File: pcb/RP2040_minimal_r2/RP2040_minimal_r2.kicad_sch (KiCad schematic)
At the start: 34 parts, among them J1 USB_B_Micro, J2 Conn_01x02, J3 Conn_02x18_Odd_Even, J4 Conn_02x18_Odd_Even, U1 NCP1117-3.3_SOT223, U2 W25Q128JVS, U3 RP2040, Y1 ABM8-272-T3

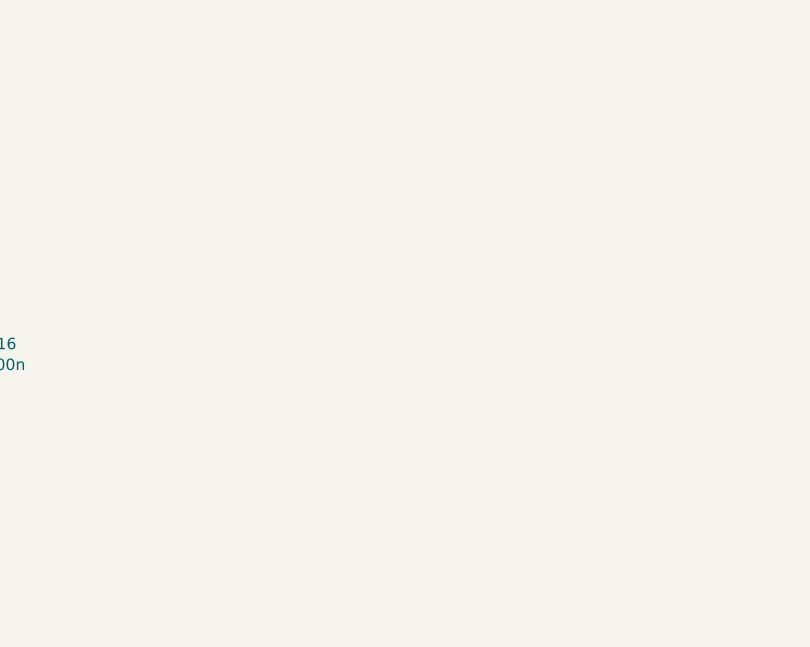
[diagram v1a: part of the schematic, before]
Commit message: add ddr contacts to pcb
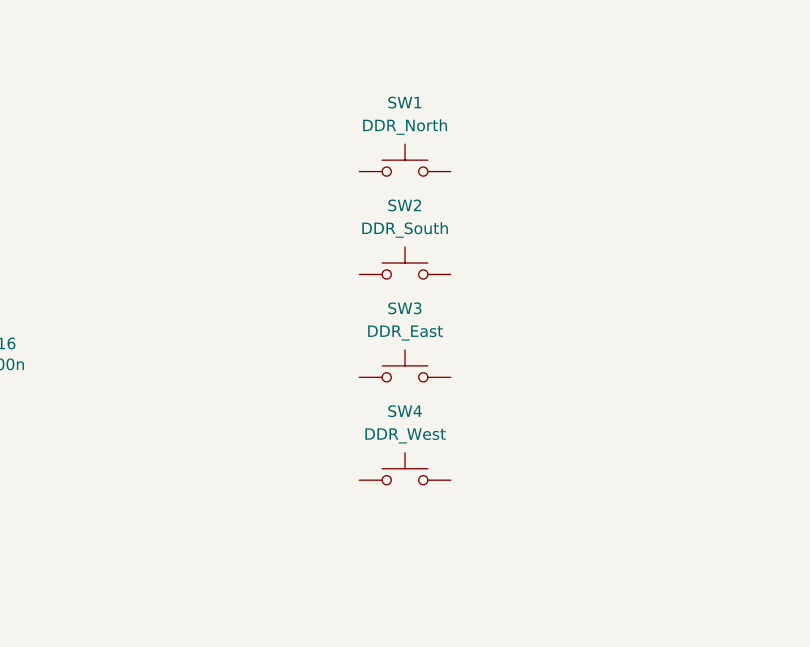
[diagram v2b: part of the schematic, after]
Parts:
- added SW1: DDR_North, Andrews_Library:DDR_CONTACT, symbol Switch:SW_Push
- added SW2: DDR_South, Andrews_Library:DDR_CONTACT, symbol Switch:SW_Push
- added SW3: DDR_East, Andrews_Library:DDR_CONTACT, symbol Switch:SW_Push
- added SW4: DDR_West, Andrews_Library:DDR_CONTACT, symbol Switch:SW_Push

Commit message: clean up pcb
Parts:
- removed H1, H2, H3, H4: MountingHole, MountingHole:MountingHole_2.7mm_M2.5, symbol Mechanical:MountingHole
- removed J3, J4: Conn_02x18_Odd_Even, Connector_PinHeader_2.54mm:PinHeader_2x18_P2.54mm_Vertical, symbol Connector_Generic:Conn_02x18_Odd_Even
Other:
- note removed: "IOs"

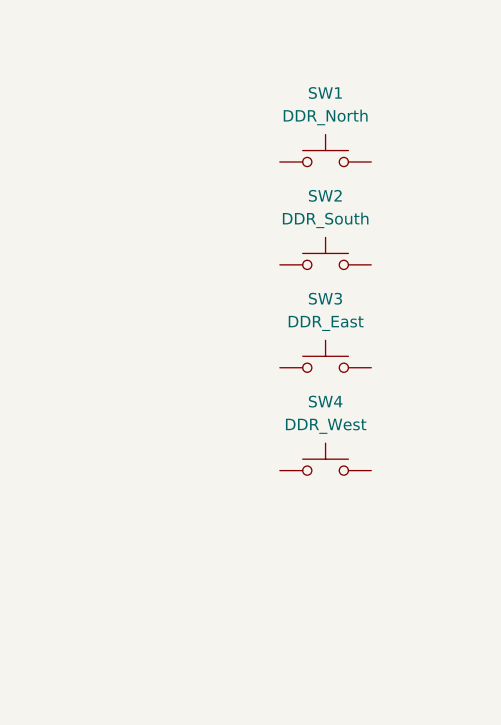
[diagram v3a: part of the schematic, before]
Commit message: add gnd zone
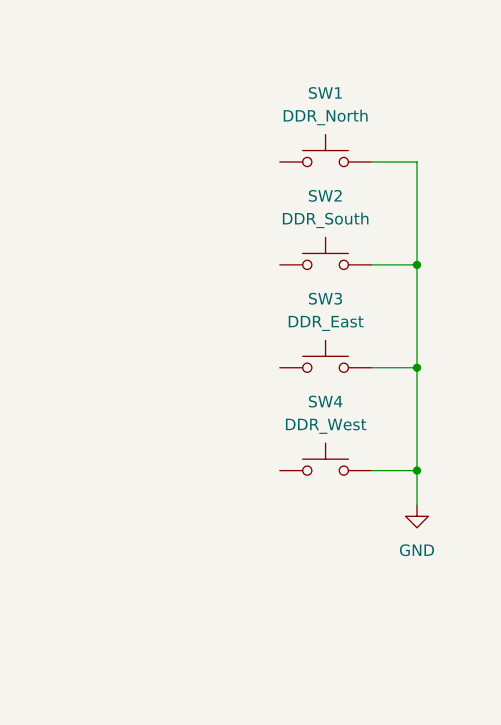
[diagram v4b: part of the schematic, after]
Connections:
- net GND: now also SW1.2, SW2.2, SW3.2, SW4.2
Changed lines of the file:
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@@
 	)
 	(junction
+		(at 351.79 68.58)
+		(diameter 0)
+		(color 0 0 0 0)
+	)
+	(junction
 		(at 177.8 60.96)
 		(diameter 0)
@@
 	)
 	(junction
+		(at 351.79 80.01)
+		(diameter 0)
+		(color 0 0 0 0)
+	)
+	(junction
 		(at 207.01 81.28)
 		(diameter 0)
@@
 	)
 	(junction
+		(at 351.79 57.15)
+		(diameter 0)
+		(color 0 0 0 0)
+	)
+	(junction
 		(at 196.85 81.28)
 		(diameter 0)
@@
 	(wire
 		(pts
+			(xy 346.71 57.15) (xy 351.79 57.15)
+		)
+		(stroke
+			(width 0)
+			(type default)
+		)
+	)
+	(wire
+		(pts
 			(xy 177.8 81.28) (xy 177.8 93.98)
 		)
@@
 	(wire
 		(pts
+			(xy 346.71 45.72) (xy 351.79 45.72)
+		)
+		(stroke
+			(width 0)
+			(type default)
+		)
+	)
+	(wire
+		(pts
 			(xy 97.79 101.6) (xy 97.79 105.41)
 		)
@@
 	(wire
 		(pts
+			(xy 351.79 68.58) (xy 351.79 80.01)
+		)
+		(stroke
+			(width 0)
+			(type default)
+		)
+	)
+	(wire
+		(pts
 			(xy 185.42 93.98) (xy 185.42 81.28)
 		)
@@
 	(wire
 		(pts
+			(xy 346.71 80.01) (xy 351.79 80.01)
+		)
+		(stroke
+			(width 0)
+			(type default)
+		)
+	)
+	(wire
+		(pts
 			(xy 152.4 119.38) (xy 166.37 119.38)
 		)
@@
 	(wire
 		(pts
+			(xy 351.79 45.72) (xy 351.79 57.15)
+		)
+		(stroke
+			(width 0)
+			(type default)
+		)
+	)
+	(wire
+		(pts
 			(xy 292.1 62.23) (xy 292.1 60.96)
 		)
@@
 	(wire
 		(pts
+			(xy 351.79 80.01) (xy 351.79 83.82)
+		)
+		(stroke
+			(width 0)
+			(type default)
+		)
+	)
+	(wire
+		(pts
 			(xy 229.87 142.24) (xy 245.11 142.24)
 		)
@@
 	(wire
 		(pts
+			(xy 351.79 57.15) (xy 351.79 68.58)
+		)
+		(stroke
+			(width 0)
+			(type default)
+		)
+	)
+	(wire
+		(pts
 			(xy 223.52 77.47) (xy 223.52 76.2)
 		)
@@
 	(wire
 		(pts
+			(xy 346.71 68.58) (xy 351.79 68.58)
+		)
+		(stroke
+			(width 0)
+			(type default)
+		)
+	)
+	(wire
+		(pts
 			(xy 280.67 60.96) (xy 292.1 60.96)
 		)
@@
 					(unit 1)
 				)
+			)
+		)
+	)
+	(symbol
+		(lib_name "GND_1")
+		(lib_id "power:GND")
+		(at 351.79 83.82 0)
+		(unit 1)
+		(body_style 1)
+		(exclude_from_sim no)
+		(in_bom yes)
+		(on_board yes)
+		(in_pos_files yes)
+		(dnp no)
+		(fields_autoplaced yes)
+		(property "Reference" "#PWR019"
+			(at 351.79 90.17 0)
+			(hide yes)
+			(show_name no)
+			(do_not_autoplace no)
+			(effects
+				(font
+					(size 1.27 1.27)
+				)
+			)
+		)
+		(property "Value" "GND"
+			(at 351.79 88.9 0)
+			(show_name no)
+			(do_not_autoplace no)
+			(effects
+				(font
+					(size 1.27 1.27)
+				)
+			)
+		)
+		(property "Footprint" ""
+			(at 351.79 83.82 0)
+			(hide yes)
+			(show_name no)
+			(do_not_autoplace no)
+			(effects
+				(font
+					(size 1.27 1.27)
+				)
+			)
+		)
+		(property "Datasheet" ""
+			(at 351.79 83.82 0)
+			(hide yes)
+			(show_name no)
+			(do_not_autoplace no)
+			(effects
+				(font
+					(size 1.27 1.27)
+				)
+			)
+		)
+		(property "Description" "Power symbol creates a global label with name \"GND\" , ground"
+			(at 351.79 83.82 0)
+			(hide yes)
+			(show_name no)
+			(do_not_autoplace no)
+			(effects
+				(font
+					(size 1.27 1.27)
+				)
+			)
+		)
+		(pin "1"
+		)
+		(instances
+			(project "RP2040_minimal_r2"
+				(path "/8c0b3d8b-46d3-4173-ab1e-a61765f77d61"
+					(reference "#PWR019")
+					(unit 1)
+				)

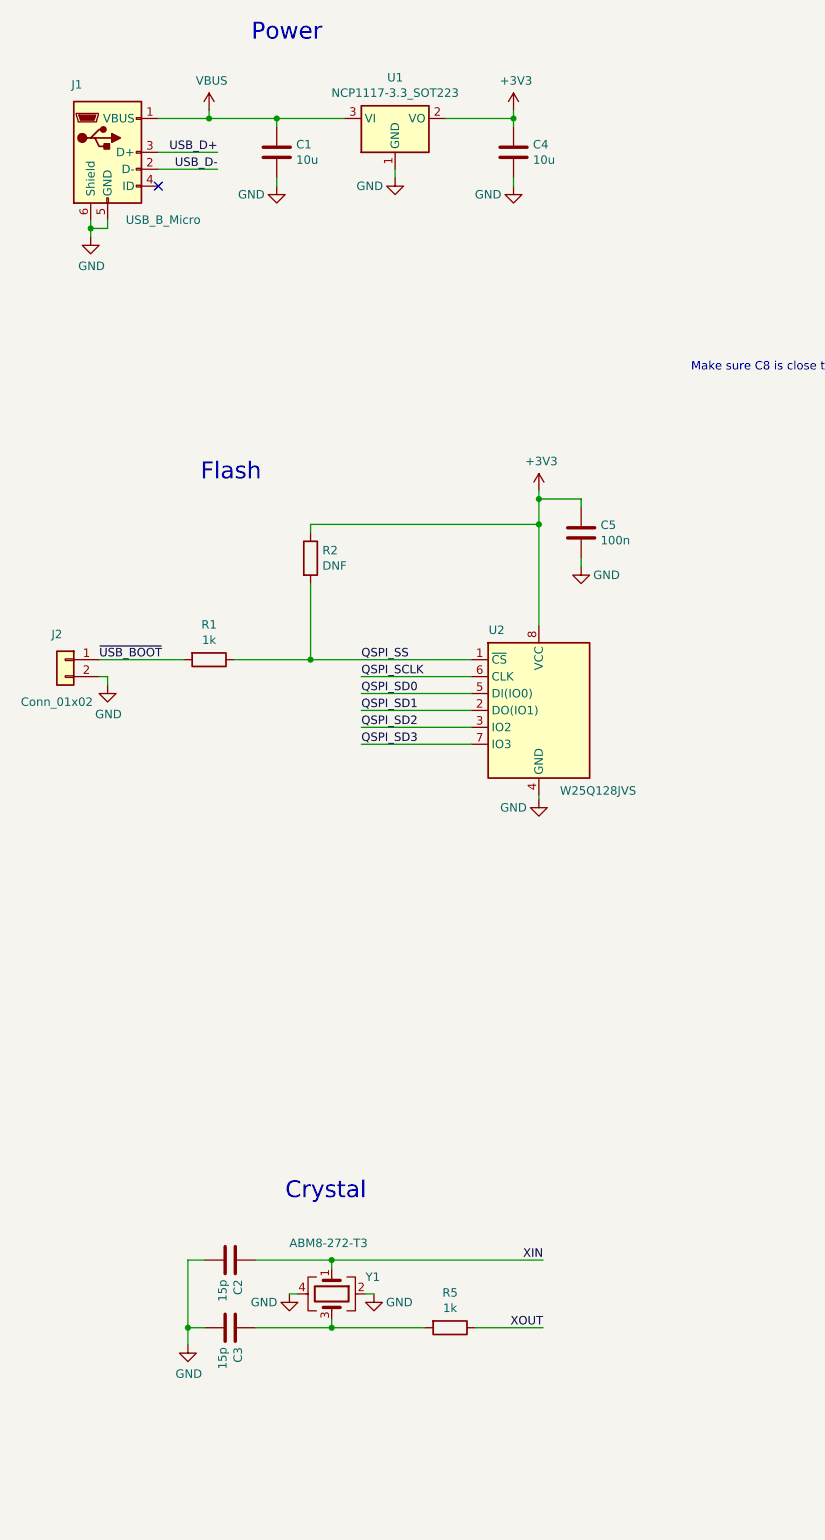
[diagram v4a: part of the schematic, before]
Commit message: add usbc to schematic
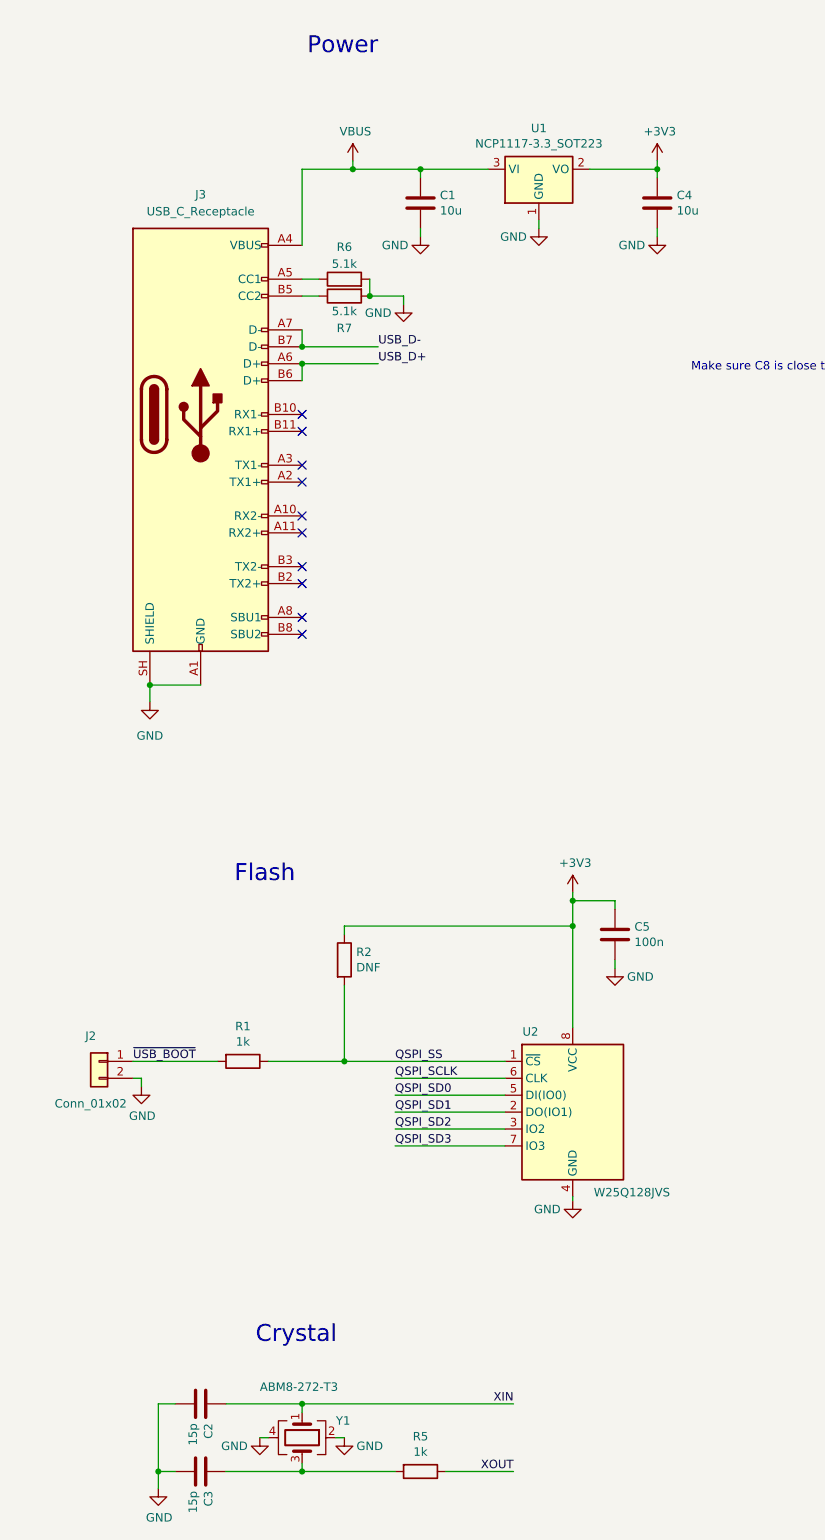
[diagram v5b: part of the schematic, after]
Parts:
- removed J1: USB_B_Micro, RP2040_minimal:USB_Micro-B_Amphenol_10103594-0001LF_Horizontal_modified, symbol Connector:USB_B_Micro
- added J3: USB_C_Receptacle, Connector_USB:USB_C_Receptacle_GCT_USB4105-xx-A_16P_TopMnt_Horizontal, symbol Connector:USB_C_Receptacle
- added R6, R7: 5.1k, Resistor_SMD:R_0402_1005Metric, symbol Device:R
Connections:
- net GND: now also J3.A1 (GND), J3.A12 (GND), J3.B1 (GND), J3.B12 (GND), J3.SH (SHIELD), R6.2, R7.2
- net USB_D+: now also J3.A6 (D+), J3.B6 (D+)
- net USB_D-: now also J3.A7 (D-), J3.B7 (D-)
- net VBUS: now also J3.A4 (VBUS), J3.A9 (VBUS), J3.B4 (VBUS), J3.B9 (VBUS)
- new net: J3.B5 (CC2), R7.1
- new net: J3.A5 (CC1), R6.1
- no-connect marks 1 -> 10
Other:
- moved on the sheet: C1, C2, C3, C4, C5, J2, R1, R2, R5, U1, U2, Y1

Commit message: finish pcb i think
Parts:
- SW1: footprint Andrews_Library:DDR_CONTACT -> Andrews_Library:DDR_CONTACT_MIRROR
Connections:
- net GPIO11: now also SW4.1
- net GPIO23: now also SW2.1
- net GPIO24: now also SW3.1
- net GPIO25: now also SW1.1
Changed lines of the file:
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@@
 	(wire
 		(pts
+			(xy 332.74 68.58) (xy 336.55 68.58)
+		)
+		(stroke
+			(width 0)
+			(type default)
+		)
+	)
+	(wire
+		(pts
 			(xy 102.87 160.655) (xy 102.87 161.925)
 		)
@@
 	(wire
 		(pts
+			(xy 332.74 45.72) (xy 336.55 45.72)
+		)
+		(stroke
+			(width 0)
+			(type default)
+		)
+	)
+	(wire
+		(pts
 			(xy 55.88 242.57) (xy 57.15 242.57)
 		)
@@
 	(wire
 		(pts
+			(xy 332.74 57.15) (xy 336.55 57.15)
+		)
+		(stroke
+			(width 0)
+			(type default)
+		)
+	)
+	(wire
+		(pts
 			(xy 214.63 59.69) (xy 214.63 60.96)
 		)
@@
 	(wire
 		(pts
+			(xy 332.74 80.01) (xy 336.55 80.01)
+		)
+		(stroke
+			(width 0)
+			(type default)
+		)
+	)
+	(wire
+		(pts
 			(xy 109.22 163.195) (xy 109.22 161.925)
 		)
@@
 		)
 	)
+	(label "GPIO11"
+		(at 332.74 80.01 180)
+		(effects
+			(font
+				(size 1.27 1.27)
+			)
+			(justify right bottom)
+		)
+	)
 	(label "QSPI_SS"
 		(at 76.2 186.055 0)
@@
 		)
 	)
+	(label "GPIO24"
+		(at 332.74 68.58 180)
+		(effects
+			(font
+				(size 1.27 1.27)
+			)
+			(justify right bottom)
+		)
+	)
 	(label "GPIO0"
 		(at 245.11 111.76 180)
@@
 		)
 	)
+	(label "GPIO23"
+		(at 332.74 57.15 180)
+		(effects
+			(font
+				(size 1.27 1.27)
+			)
+			(justify right bottom)
+		)
+	)
 	(label "SWCLK"
 		(at 152.4 176.53 0)
@@
 		)
 	)
+	(label "GPIO25"
+		(at 332.74 45.72 180)
+		(effects
+			(font
+				(size 1.27 1.27)
+			)
+			(justify right bottom)
+		)
+	)
 	(label "QSPI_SS"
 		(at 152.4 113.03 0)
@@
 			)
 		)
-		(property "Footprint" "Andrews_Library:DDR_CONTACT"
+		(property "Footprint" "Andrews_Library:DDR_CONTACT_MIRROR"
 			(at 341.63 40.64 0)
 			(hide yes)
